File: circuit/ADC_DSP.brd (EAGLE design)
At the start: 64.8 x 76.8 mm, 76 parts, among them IC1 REG1117, IC3 STM32F40XRXT6, IC4 CS4272, Q1 8MHz, Q2 24.576MHz

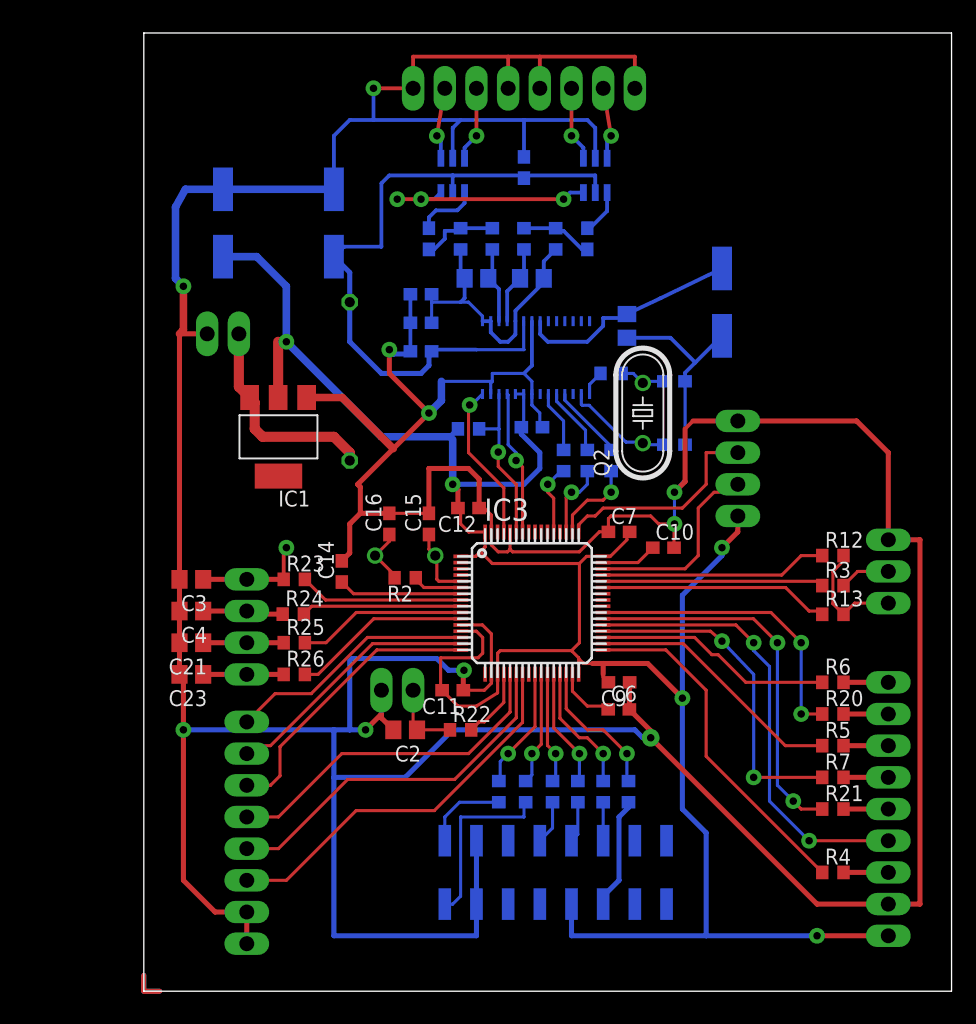
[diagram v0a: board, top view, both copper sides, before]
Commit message: - уменьшили ширину платы
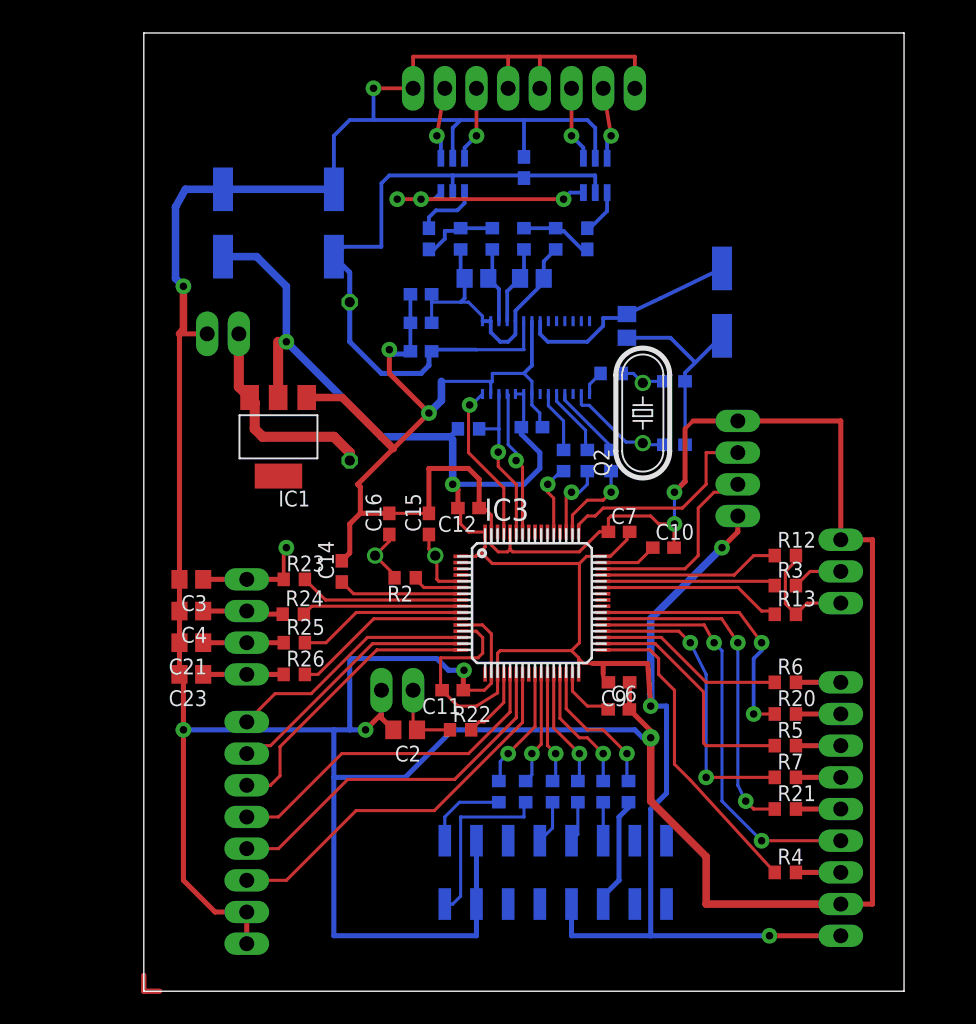
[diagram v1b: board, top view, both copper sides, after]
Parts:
- moved LCD 3.81 mm to (55.9, 14.6)
- moved R12 3.81 mm to (51.4, 34.9)
- moved R13 3.81 mm to (51.4, 30.2)
- moved R20 3.81 mm to (51.4, 22.2)
- moved R21 3.81 mm to (51.4, 14.6)
- moved R3 3.81 mm to (51.4, 32.5)
- moved R4 3.81 mm to (51.4, 9.53)
- moved R5 3.81 mm to (51.4, 19.7)
- moved R6 3.81 mm to (51.4, 24.8)
- moved R7 3.81 mm to (51.4, 17.1)
- moved USB 3.81 mm to (55.9, 33.7)
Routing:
- net USB_DP: track 18.2 -> 14.4 mm
- net PB14(TFT_MISO): track 19.1 -> 15.3 mm
- net USB_DM: track 17.7 -> 13.9 mm
- net PA10(USB_ON): track 18.5 -> 14.7 mm
- net PC7(TFT_D_C): track 30.6 -> 27.3 mm
- net PB15(TFT_MOSI): track 27.3 -> 24.0 mm
- net PC6(TFT_RESET): track 36.7 -> 33.5 mm
- net PC8(TFT_LED): track 24.3 -> 21.6 mm
- net PB12(TFT_CS): track 28.1 -> 25.6 mm
- net +3V3: track 183.4 -> 181.2 mm
- net PB13(TFT_SCK): track 21.0 -> 19.6 mm
- net GND: track 470.6 -> 469.7 mm
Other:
- board size 64.8 x 76.8 mm -> 61 x 76.8 mm

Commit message: - плата, которую будем травить
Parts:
- R28, R29: value 1.2k -> 120
- moved R1 3.47 mm to (39.4, 46.6)
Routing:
- net N$46: track 0.00 -> 3.81 mm
- net N$43: track 0.00 -> 3.81 mm
- net N$47: track 0.00 -> 3.81 mm
- net N$42: track 0.00 -> 3.81 mm
- net N$45: track 0.00 -> 2.54 mm
- net N$44: track 0.00 -> 2.54 mm
- net N$17: track 2.01 -> 3.29 mm
- net GND: vias 10 -> 13
- added copper zone on layer 1, net GND
- added copper zone on layer 16, net GND
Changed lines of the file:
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@@
 <layer number="19" name="Unrouted" color="6" fill="1" visible="yes" active="yes"/>
 <layer number="20" name="Dimension" color="15" fill="1" visible="yes" active="yes"/>
-<layer number="21" name="tPlace" color="7" fill="1" visible="yes" active="yes"/>
-<layer number="22" name="bPlace" color="7" fill="1" visible="yes" active="yes"/>
+<layer number="21" name="tPlace" color="7" fill="1" visible="no" active="yes"/>
+<layer number="22" name="bPlace" color="7" fill="1" visible="no" active="yes"/>
 <layer number="23" name="tOrigins" color="15" fill="1" visible="yes" active="yes"/>
 <layer number="24" name="bOrigins" color="15" fill="1" visible="yes" active="yes"/>
 <layer number="25" name="tNames" color="7" fill="1" visible="no" active="yes"/>
-<layer number="26" name="bNames" color="7" fill="1" visible="yes" active="yes"/>
+<layer number="26" name="bNames" color="7" fill="1" visible="no" active="yes"/>
 <layer number="27" name="tValues" color="7" fill="1" visible="no" active="yes"/>
 <layer number="28" name="bValues" color="7" fill="1" visible="no" active="yes"/>
@@
 <element name="C28" library="rcl" package="C0805" value="1.5n" x="26.67" y="57.15" rot="MR0"/>
 <element name="C5" library="rcl" package="153CLV-0605" value="220uF" x="6.35" y="61.595" rot="MR270"/>
-<element name="R1" library="rcl" package="R0603" value="220" x="37.465" y="49.53" rot="MR0"/>
+<element name="R1" library="rcl" package="R0603" value="220" x="39.35" y="46.615" rot="MR0"/>
 <element name="R2" library="rcl" package="R0603" value="220" x="20.955" y="33.145" rot="R180"/>
 <element name="C1" library="rcl" package="153CLV-0605" value="33uF" x="46.355" y="55.245" rot="MR90"/>
@@
 <attribute name="OC_FARNELL" value="unknown" x="55.88" y="33.655" size="1.778" layer="28" rot="MR90" display="off"/>
 </element>
-<element name="R28" library="rcl" package="R0603" value="1.2k" x="30.48" y="60.325" rot="MR90"/>
-<element name="R29" library="rcl" package="R0603" value="1.2k" x="27.94" y="60.325" rot="MR90"/>
+<element name="R28" library="rcl" package="R0603" value="120" x="30.48" y="60.325" rot="MR90"/>
+<element name="R29" library="rcl" package="R0603" value="120" x="27.94" y="60.325" rot="MR90"/>
 <element name="R32" library="rcl" package="R0603" value="10k" x="25.4" y="60.325" rot="MR90"/>
 <element name="R34" library="rcl" package="R0603" value="10k" x="33.02" y="60.325" rot="MR90"/>
@@
 <wire x1="45.085" y1="10.795" x2="45.085" y2="6.985" width="0.6096" layer="1"/>
 <wire x1="45.085" y1="6.985" x2="55.88" y2="6.985" width="0.6096" layer="1"/>
+<polygon width="0.4064" layer="16" isolate="0.4064">
+<vertex x="0" y="77.47"/>
+<vertex x="60.96" y="77.47"/>
+<vertex x="60.96" y="-0.635"/>
+<vertex x="0" y="-0.635"/>
+</polygon>
+<polygon width="0.4064" layer="1" isolate="0.4064">
+<vertex x="0" y="77.47"/>
+<vertex x="60.96" y="77.47"/>
+<vertex x="60.96" y="-0.635"/>
+<vertex x="0" y="-0.635"/>
+</polygon>
+<via x="3" y="74" extent="1-16" drill="0.6" diameter="1.016"/>
+<via x="57.96" y="74" extent="1-16" drill="0.6" diameter="1.016"/>
+<via x="3" y="3" extent="1-16" drill="0.6" diameter="1.016"/>
+<wire x1="5.715" y1="6.35" x2="3" y2="3" width="0" layer="19" extent="1-1"/>
 </signal>
 <signal name="+3V3">
@@
 <contactref element="IC4" pad="1"/>
 <contactref element="R1" pad="2"/>
-<wire x1="35.7378" y1="47.879" x2="35.7378" y2="48.6528" width="0.25" layer="16"/>
-<wire x1="35.7378" y1="48.6528" x2="36.615" y2="49.53" width="0.25" layer="16"/>
+<wire x1="35.7378" y1="47.879" x2="37.236" y2="47.879" width="0.3048" layer="16"/>
+<wire x1="37.236" y1="47.879" x2="38.5" y2="46.615" width="0.3048" layer="16"/>
 </signal>
 <signal name="N$8">
@@
 <contactref element="C18" pad="2"/>
 <contactref element="Q2" pad="2"/>
-<wire x1="38.315" y1="49.53" x2="39.243" y2="49.53" width="0.25" layer="16"/>
-<wire x1="39.243" y1="49.53" x2="40.005" y2="48.768" width="0.25" layer="16"/>
-<wire x1="41.695" y1="48.895" x2="40.132" y2="48.895" width="0.25" layer="16"/>
-<wire x1="40.132" y1="48.895" x2="40.005" y2="48.768" width="0.25" layer="16"/>
+<wire x1="40.2" y1="46.615" x2="40.2" y2="48.26" width="0.3048" layer="16"/>
+<wire x1="40.2" y1="48.26" x2="40.2" y2="48.573" width="0.3048" layer="16"/>
+<wire x1="40.2" y1="48.573" x2="40.005" y2="48.768" width="0.3048" layer="16"/>
+<wire x1="41.695" y1="48.895" x2="40.835" y2="48.895" width="0.3048" layer="16"/>
+<wire x1="40.835" y1="48.895" x2="40.2" y2="48.26" width="0.3048" layer="16"/>
 </signal>
 <signal name="N$19">
@@
 <wire x1="11.215" y1="35.345" x2="11.43" y2="35.56" width="0.3048" layer="1"/>
 <via x="11.43" y="35.56" extent="1-16" drill="0.6" diameter="1.27"/>
-<wire x1="11.43" y1="35.56" x2="16.51" y2="50.8" width="0" layer="19" extent="1-16"/>
-<wire x1="16.51" y1="50.8" x2="20.32" y2="63.5" width="0" layer="19" extent="1-16"/>
 <via x="20.32" y="63.5" extent="1-16" drill="0.6" diameter="1.27"/>
 <wire x1="20.32" y1="63.5" x2="22.225" y2="63.5" width="0.3048" layer="1"/>
+<wire x1="11.43" y1="35.56" x2="20.32" y2="63.5" width="0" layer="19" extent="1-1"/>
 </signal>
 <signal name="4052_B">
@@
 <wire x1="23.495" y1="68.58" x2="24.13" y2="72.39" width="0.3048" layer="1"/>
 </signal>
+<signal name="N$42">
+<wire x1="1.905" y1="76.835" x2="0" y2="76.835" width="0.4064" layer="1"/>
+<wire x1="0" y1="76.835" x2="0" y2="74.93" width="0.4064" layer="1"/>
+</signal>
+<signal name="N$43">
+<wire x1="59.055" y1="76.835" x2="60.96" y2="76.835" width="0.4064" layer="1"/>
+<wire x1="60.96" y1="76.835" x2="60.96" y2="74.93" width="0.4064" layer="1"/>
+</signal>
+<signal name="N$44">
+<wire x1="59.69" y1="0" x2="60.96" y2="0" width="0.4064" layer="1"/>
+<wire x1="60.96" y1="0" x2="60.96" y2="1.27" width="0.4064" layer="1"/>
+</signal>
+<signal name="N$45">
+<wire x1="59.69" y1="0" x2="60.96" y2="0" width="0.4064" layer="16"/>
+<wire x1="60.96" y1="0" x2="60.96" y2="1.27" width="0.4064" layer="16"/>
+</signal>
+<signal name="N$46">
+<wire x1="59.055" y1="76.835" x2="60.96" y2="76.835" width="0.4064" layer="16"/>
+<wire x1="60.96" y1="76.835" x2="60.96" y2="74.93" width="0.4064" layer="16"/>
+</signal>
+<signal name="N$47">
+<wire x1="1.905" y1="76.835" x2="0" y2="76.835" width="0.4064" layer="16"/>
+<wire x1="0" y1="76.835" x2="0" y2="74.93" width="0.4064" layer="16"/>
+</signal>
 </signals>

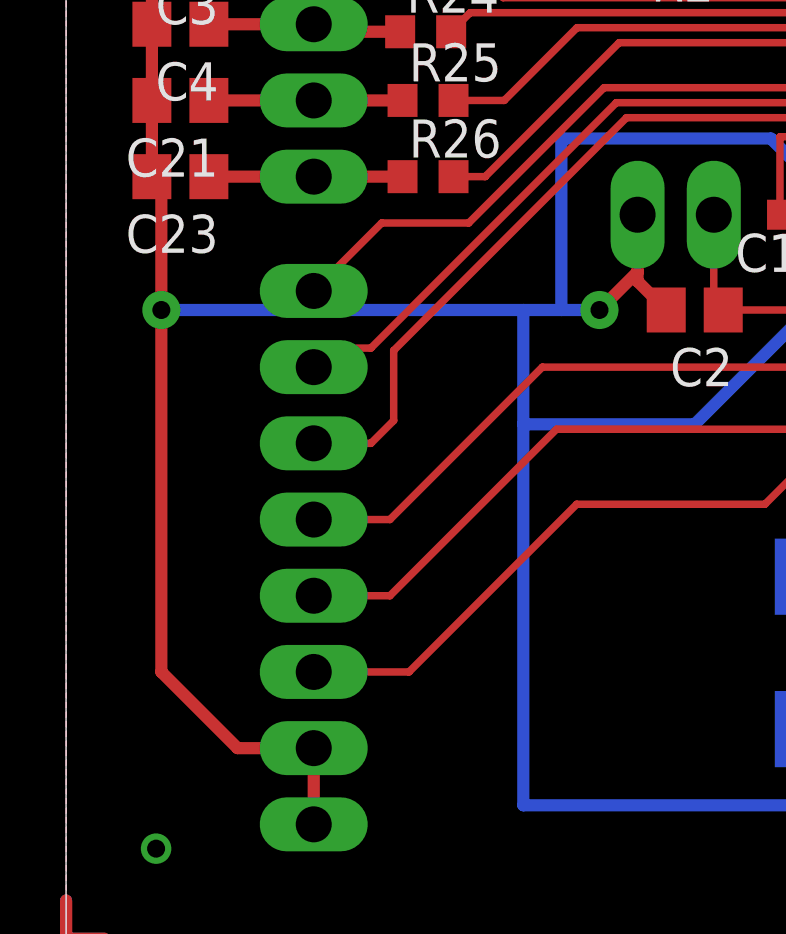
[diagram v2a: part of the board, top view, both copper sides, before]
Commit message: - один из проводов пересекался с другим
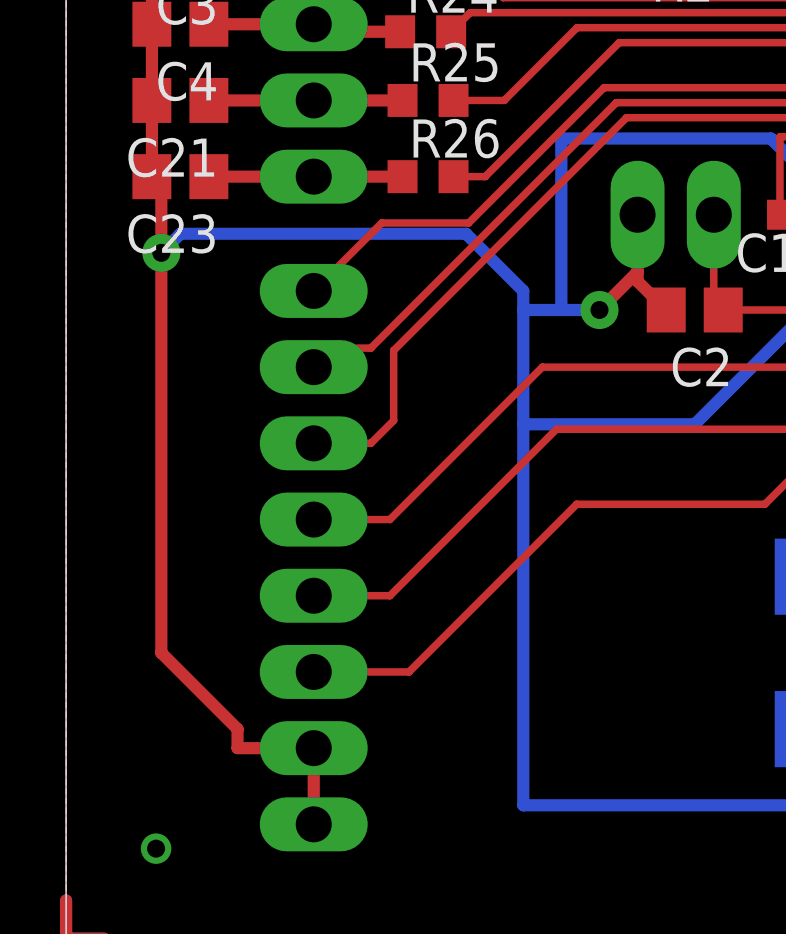
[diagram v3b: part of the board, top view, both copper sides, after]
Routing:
- net GND: track 469.7 -> 471.3 mm

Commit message: - работающий DDS
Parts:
- C25, C35: value 2.2u -> 1u
- C27, C28: value 1.5n -> 4.7n
- R28, R29: value 120 -> 150
- R32, R34: value 10k -> 12k

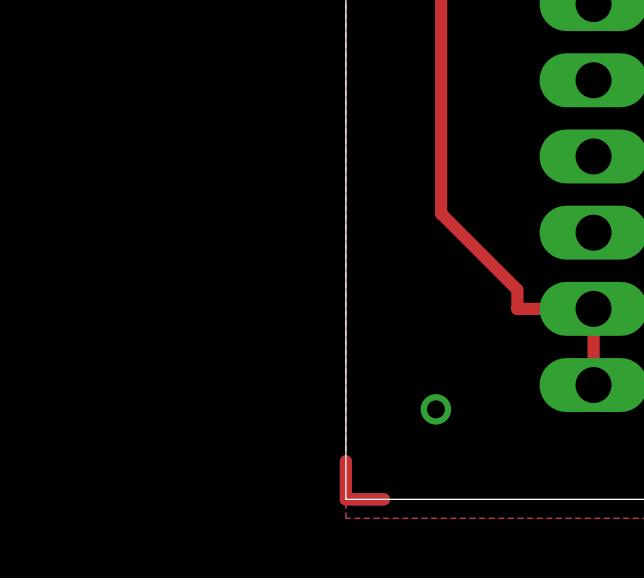
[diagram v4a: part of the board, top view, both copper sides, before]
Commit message: - была ошибка в TimeMs() - конденсатор 100 uF на VCOM - не успевает выводить на дисплей и обрабатывать звук.
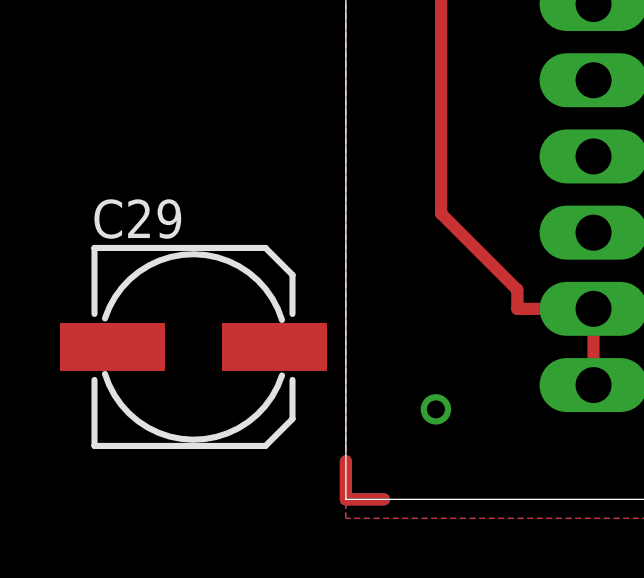
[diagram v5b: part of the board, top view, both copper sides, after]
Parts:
- added C29: 100uF, rcl:153CLV-0605
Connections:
- net GND: now also C29.-
- net VCOM: now also C29.+
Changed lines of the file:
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@@
 </element>
 <element name="C13" library="rcl" package="C0603" value="100n" x="30.48" y="66.04" rot="MR90"/>
+<element name="C29" library="rcl" package="153CLV-0605" value="100uF" x="-5.08" y="5.08"/>
 </elements>
 <signals>
@@
 <wire x1="5.715" y1="6.985" x2="3.175" y2="9.525" width="0.4064" layer="1"/>
 <wire x1="3.175" y1="9.525" x2="3.175" y2="22.86" width="0.4064" layer="1"/>
+<contactref element="C29" pad="-"/>
+<wire x1="39.37" y1="74.93" x2="57.96" y2="74" width="0" layer="19" extent="1-1"/>
+<wire x1="3" y1="3" x2="5.715" y2="6.35" width="0" layer="19" extent="1-1"/>
+<wire x1="3" y1="74" x2="3.335" y2="64.295" width="0" layer="19" extent="16-16"/>
+<wire x1="-7.78" y1="5.08" x2="3" y2="3" width="0" layer="19" extent="1-1"/>
 </signal>
 <signal name="+3V3">
@@
 <wire x1="25.4" y1="59.475" x2="25.4" y2="57.47" width="0.3048" layer="16"/>
 <wire x1="25.4" y1="57.47" x2="25.72" y2="57.15" width="0.3048" layer="16"/>
+<contactref element="C29" pad="+"/>
+<wire x1="-2.38" y1="5.08" x2="23.075" y2="53.59" width="0" layer="19" extent="1-16"/>
 </signal>
 <signal name="AVCC">
